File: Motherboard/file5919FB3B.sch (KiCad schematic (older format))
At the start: 19 parts, among them P301 USB_OTG, SW301 SW_PUSH, U301 FT232RL

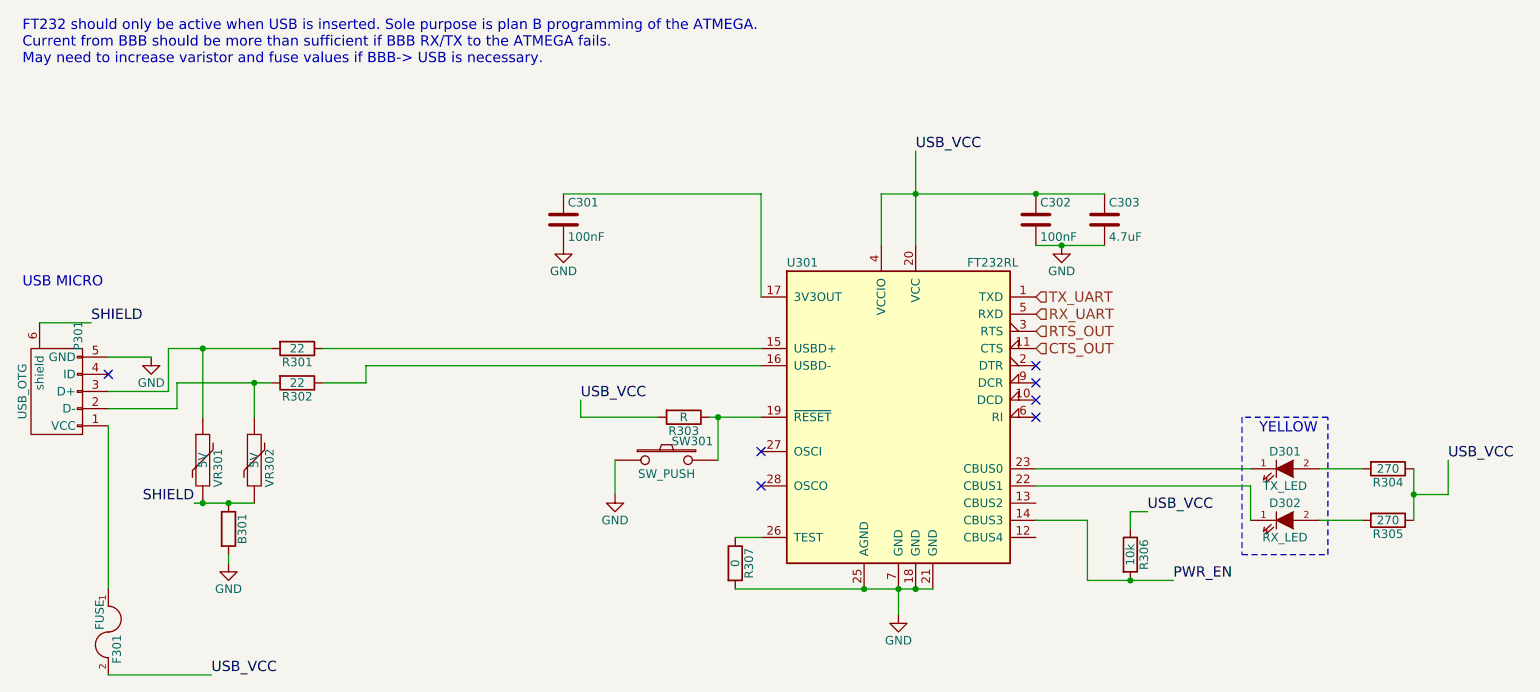
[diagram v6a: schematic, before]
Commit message: Mobo Version 2.1 Added Silk scren Ground Plane Cleanup Pinout changes on Beaglebone Headers, need to modify cabeling from V2.0 and earlier Added power sequencing for ADCs Removed Y3 ADC Removed TI Battery Board I2C lines More 5V connectors on Board Adjusted ADC Connecter pinout to match interface modules
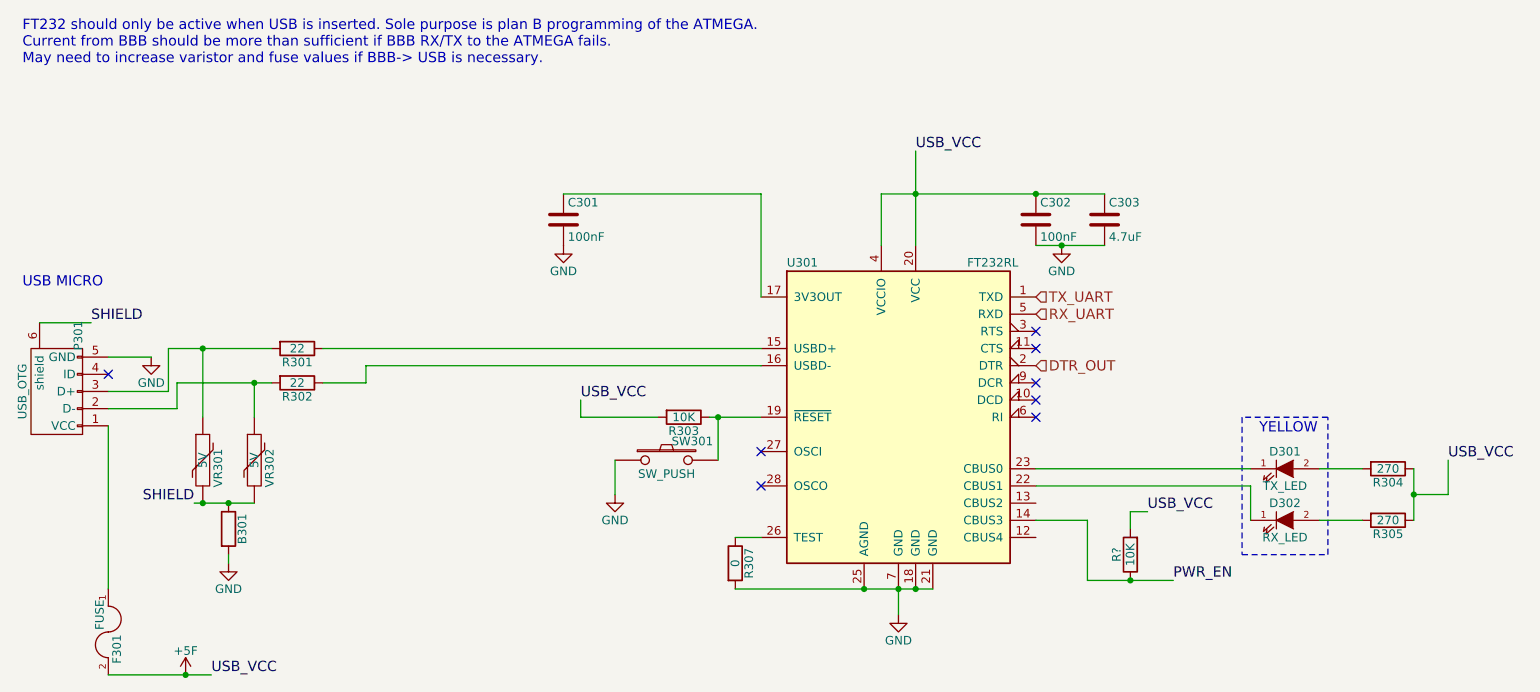
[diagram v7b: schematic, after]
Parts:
- removed R306: 10k, Resistors_SMD:R_0805_HandSoldering, symbol R
- added R?: 10K, Resistors_SMD:R_0805_HandSoldering, symbol R
- C301: Digikey P/N (none) -> 490-10510-1-ND; Mfr P/N (none) -> GRM21BR60G107ME15L
- R301, R302: footprint Resistors_SMD:R_0805_HandSoldering -> Resistors_SMD:R_0603_HandSoldering; Digikey P/N 311-22ARCT-ND -> 311-22GRCT-ND; MFR P/N RC0805JR-0722RL -> RC0603JR-0722RL
- R303: value R -> 10K; Digikey P/N (none) -> 311-10KARCT-ND; Mfr P/N (none) -> RC0805JR-0710KL
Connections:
- net PWR_EN: now also R?.1
- net DTR_OUT: now reaches U301.2 (DTR)
- net CTS_OUT: no longer names the net of U301.11 (CTS)
- net RTS_OUT: no longer names the net of U301.3 (RTS)
- net USB_VCC renamed +5F
- net +5F: now also R?.2
- no-connect marks 7 -> 8
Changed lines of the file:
@@
 $Descr A4 11693 8268
 encoding utf-8
-Sheet 3 15
+Sheet 3 14
 Title "Motherboard"
-Date ""
-Rev "2"
-Comp "Paradigm Transportation"
-Comment1 ""
-Comment2 ""
+Date "2017-07-31"
+Rev "2.1"
+Comp "© 2017 Paradigm Hyperloop. All Rights Reserved"
+Comment1 "Electrical Team"
+Comment2 "Luke Merkl"
 Comment3 ""
 Comment4 ""
@@
 	0    1    1    0
 $EndComp
-Text HLabel 6500 2400 2    60   Input ~ 0
-RTS_OUT
-Text HLabel 6500 2500 2    60   Input ~ 0
-CTS_OUT
-$Comp
-L GND #PWR012
+$Comp
+L GND #PWR306
 U 1 1 591EFDC3
 P 5700 4050
-F 0 "#PWR012" H 5700 3800 50  0001 C CNN
+F 0 "#PWR306" H 5700 3800 50  0001 C CNN
 F 1 "GND" H 5700 3900 50  0000 C CNN
 F 2 "" H 5700 4050 50  0000 C CNN
@@
 F 2 "Capacitors_SMD:C_0805_HandSoldering" H 3788 1600 50  0001 C CNN
 F 3 "" H 3750 1750 50  0000 C CNN
+F 4 "490-10510-1-ND" H 3750 1750 60  0001 C CNN "Digikey P/N"
+F 5 "GRM21BR60G107ME15L" H 3750 1750 60  0001 C CNN "Mfr P/N"
 	1    3750 1750
 	1    0    0    -1
 $EndComp
 $Comp
-L GND #PWR013
+L GND #PWR301
 U 1 1 591F018C
 P 3750 1900
-F 0 "#PWR013" H 3750 1650 50  0001 C CNN
+F 0 "#PWR301" H 3750 1650 50  0001 C CNN
 F 1 "GND" H 3750 1750 50  0000 C CNN
 F 2 "" H 3750 1900 50  0000 C CNN
@@
 F 0 "R301" V 2280 2500 50  0000 C CNN
 F 1 "22" V 2200 2500 50  0000 C CNN
-F 2 "Resistors_SMD:R_0805_HandSoldering" V 2130 2500 50  0001 C CNN
+F 2 "Resistors_SMD:R_0603_HandSoldering" V 2130 2500 50  0001 C CNN
 F 3 "" H 2200 2500 50  0000 C CNN
-F 4 "311-22ARCT-ND" V 2200 2500 60  0001 C CNN "Digikey P/N"
-F 5 "RC0805JR-0722RL" V 2200 2500 60  0001 C CNN "MFR P/N"
+F 4 "311-22GRCT-ND" V 2200 2500 60  0001 C CNN "Digikey P/N"
+F 5 "RC0603JR-0722RL" V 2200 2500 60  0001 C CNN "MFR P/N"
 	1    2200 2500
 	0    1    1    0
 $EndComp
 $Comp
-L GND #PWR014
+L GND #PWR305
 U 1 1 591F12E5
 P 1800 3750
-F 0 "#PWR014" H 1800 3500 50  0001 C CNN
+F 0 "#PWR305" H 1800 3500 50  0001 C CNN
 F 1 "GND" H 1800 3600 50  0000 C CNN
 F 2 "" H 1800 3750 50  0000 C CNN
@@
 P 4450 2900
 F 0 "R303" V 4530 2900 50  0000 C CNN
-F 1 "R" V 4450 2900 50  0000 C CNN
+F 1 "10K" V 4450 2900 50  0000 C CNN
 F 2 "Resistors_SMD:R_0805_HandSoldering" V 4380 2900 50  0001 C CNN
 F 3 "" H 4450 2900 50  0000 C CNN
+F 4 "311-10KARCT-ND" V 4450 2900 60  0001 C CNN "Digikey P/N"
+F 5 "RC0805JR-0710KL" V 4450 2900 60  0001 C CNN "Mfr P/N"
 	1    4450 2900
 	0    1    1    0
@@
 	4050 3150 4050 3350
 $Comp
-L GND #PWR015
+L GND #PWR304
 U 1 1 59225F84
 P 4050 3350
-F 0 "#PWR015" H 4050 3100 50  0001 C CNN
+F 0 "#PWR304" H 4050 3100 50  0001 C CNN
 F 1 "GND" H 4050 3200 50  0000 C CNN
 F 2 "" H 4050 3350 50  0000 C CNN
 F 3 "" H 4050 3350 50  0000 C CNN
 	1    4050 3350
-	1    0    0    -1
-$EndComp
-$Comp
-L R R306
-U 1 1 59226C41
-P 7050 3700
-F 0 "R306" V 7130 3700 50  0000 C CNN
-F 1 "10k" V 7050 3700 50  0000 C CNN
-F 2 "Resistors_SMD:R_0805_HandSoldering" V 6980 3700 50  0001 C CNN
-F 3 "" H 7050 3700 50  0000 C CNN
-	1    7050 3700
 	1    0    0    -1
 $EndComp
@@
 	4750 3600 4900 3600
 $Comp
-L GND #PWR016
+L GND #PWR303
 U 1 1 5922A650
 P 1350 2550
-F 0 "#PWR016" H 1350 2300 50  0001 C CNN
+F 0 "#PWR303" H 1350 2300 50  0001 C CNN
 F 1 "GND" H 1350 2400 50  0000 C CNN
 F 2 "" H 1350 2550 50  0000 C CNN
@@
 NoConn ~ 4900 3100
 NoConn ~ 4900 3300
-NoConn ~ 6500 2600
 NoConn ~ 6500 2700
 NoConn ~ 6500 2800
@@
 	6500 1900 6900 1900
 $Comp
-L GND #PWR017
+L GND #PWR302
 U 1 1 5922B762
 P 6650 1900
-F 0 "#PWR017" H 6650 1650 50  0001 C CNN
+F 0 "#PWR302" H 6650 1650 50  0001 C CNN
 F 1 "GND" H 6650 1750 50  0000 C CNN
 F 2 "" H 6650 1900 50  0000 C CNN
@@
 Wire Notes Line
 	8200 2900 7700 2900
-$Comp
-L R R302
-U 1 1 59383E0B
-P 2200 2700
-F 0 "R302" V 2280 2700 50  0000 C CNN
-F 1 "22" V 2200 2700 50  0000 C CNN
-F 2 "Resistors_SMD:R_0805_HandSoldering" V 2130 2700 50  0001 C CNN
-F 3 "" H 2200 2700 50  0000 C CNN
-F 4 "311-22ARCT-ND" V 2200 2700 60  0001 C CNN "Digikey P/N"
-F 5 "RC0805JR-0722RL" V 2200 2700 60  0001 C CNN "MFR P/N"
-	1    2200 2700
-	0    1    1    0
-$EndComp
 Text Label 8900 3150 0    60   ~ 0
 USB_VCC
@@
 	1    0    0    -1
 $EndComp
+$Comp
+L R R302
+U 1 1 597E4FAC
+P 2200 2700
+F 0 "R302" V 2280 2700 50  0000 C CNN
+F 1 "22" V 2200 2700 50  0000 C CNN
+F 2 "Resistors_SMD:R_0603_HandSoldering" V 2130 2700 50  0001 C CNN
+F 3 "" H 2200 2700 50  0000 C CNN
+F 4 "311-22GRCT-ND" V 2200 2700 60  0001 C CNN "Digikey P/N"
+F 5 "RC0603JR-0722RL" V 2200 2700 60  0001 C CNN "MFR P/N"
+	1    2200 2700
+	0    1    1    0
+$EndComp
+Text HLabel 6500 2600 2    60   Input ~ 0
+DTR_OUT
+$Comp
+L +5F #PWR307
+U 1 1 5984B2C3
+P 1550 4400
+F 0 "#PWR307" H 1550 4250 50  0001 C CNN
+F 1 "+5F" H 1550 4540 50  0000 C CNN
+F 2 "" H 1550 4400 50  0000 C CNN
+F 3 "" H 1550 4400 50  0000 C CNN
+	1    1550 4400
+	1    0    0    -1
+$EndComp
+Connection ~ 1550 4400
+NoConn ~ 6500 2400
+NoConn ~ 6500 2500
+$Comp
+L R R?
+U 1 1 598BA583
+P 7050 3700
+F 0 "R?" V 7130 3700 50  0000 C CNN
+F 1 "10K" V 7050 3700 50  0000 C CNN
+F 2 "Resistors_SMD:R_0805_HandSoldering" V 6980 3700 50  0001 C CNN
+F 3 "" H 7050 3700 50  0000 C CNN
+F 4 "311-10KARCT-ND" V 7050 3700 60  0001 C CNN "Digikey P/N"
+F 5 "RC0805JR-0710KL" V 7050 3700 60  0001 C CNN "Mfr P/N"
+	1    7050 3700
+	-1   0    0    1
+$EndComp
 $EndSCHEMATC

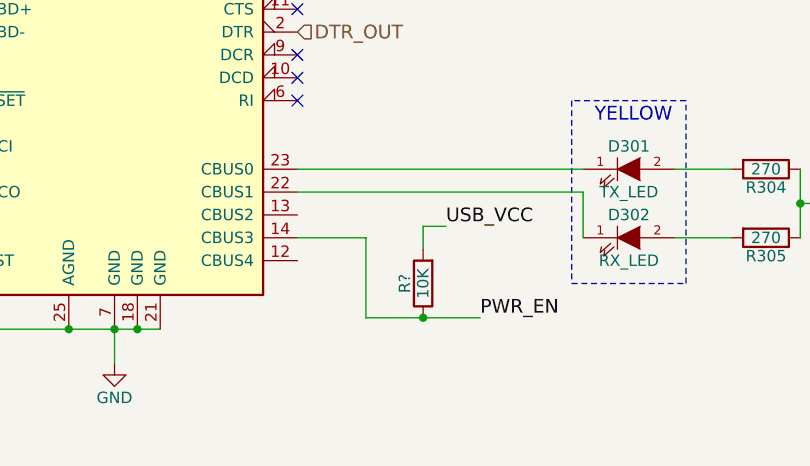
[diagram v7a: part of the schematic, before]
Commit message: Updating to kiCAD version 4.0.6. Updated some .drl files per advanced circuits hold order
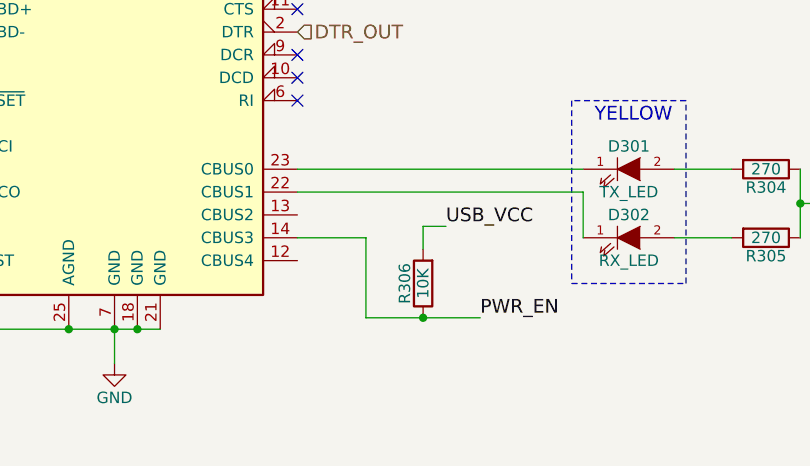
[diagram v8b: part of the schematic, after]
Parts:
- gave numbers to parts that had none: 1
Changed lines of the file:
@@
 NoConn ~ 6500 2500
 $Comp
-L R R?
+L R R306
 U 1 1 598BA583
 P 7050 3700
-F 0 "R?" V 7130 3700 50  0000 C CNN
+F 0 "R306" V 7130 3700 50  0000 C CNN
 F 1 "10K" V 7050 3700 50  0000 C CNN
 F 2 "Resistors_SMD:R_0805_HandSoldering" V 6980 3700 50  0001 C CNN
